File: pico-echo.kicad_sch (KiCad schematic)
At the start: 51 parts, among them J1 USB_C_Receptacle_USB2.0, J2 I2C, J4 Conn_01x16, J5 Conn_01x12, J6 BAT, Q1 BSS83P, SW1 SW_Push, SW2 SW_Push, U1 RP2040, U2 W25Q128JVS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

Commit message: Updated tracks, not finished yet
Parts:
- D2: footprint Capacitor_SMD:C_0603_1608Metric -> LED_SMD:LED_0603_1608Metric
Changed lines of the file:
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@@
 			)
 		)
-		(property "Footprint" "Capacitor_SMD:C_0603_1608Metric"
+		(property "Footprint" "LED_SMD:LED_0603_1608Metric"
 			(at 107.95 39.37 0)
 			(effects

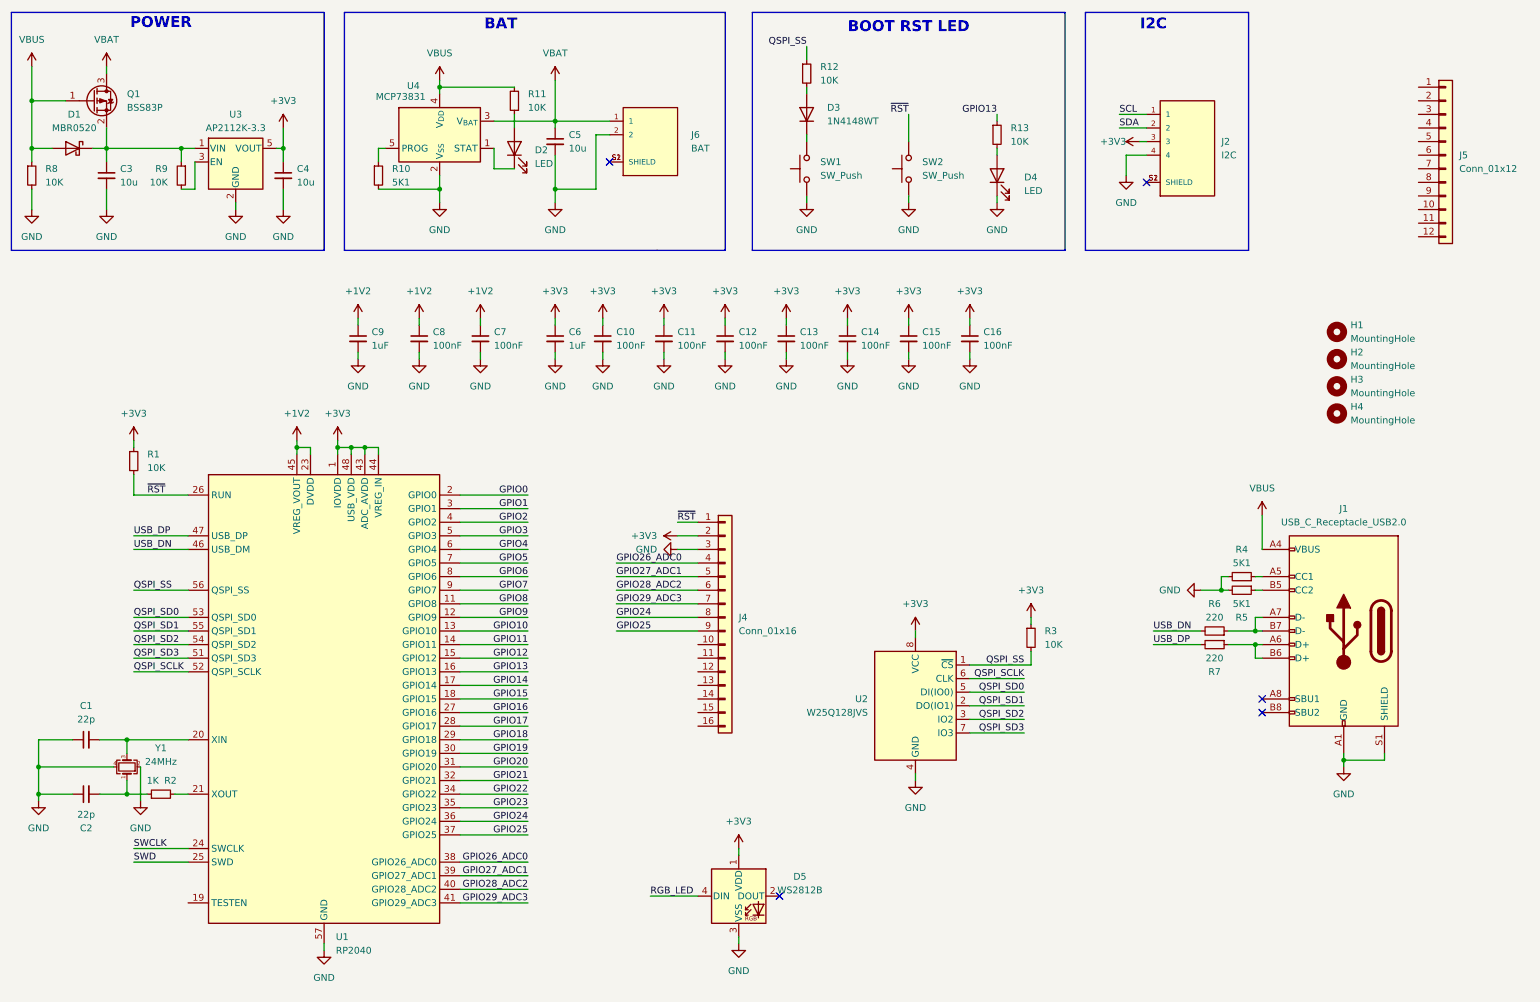
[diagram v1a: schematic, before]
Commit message: Add SWD conn, change Flash to USON, tracks almost finished
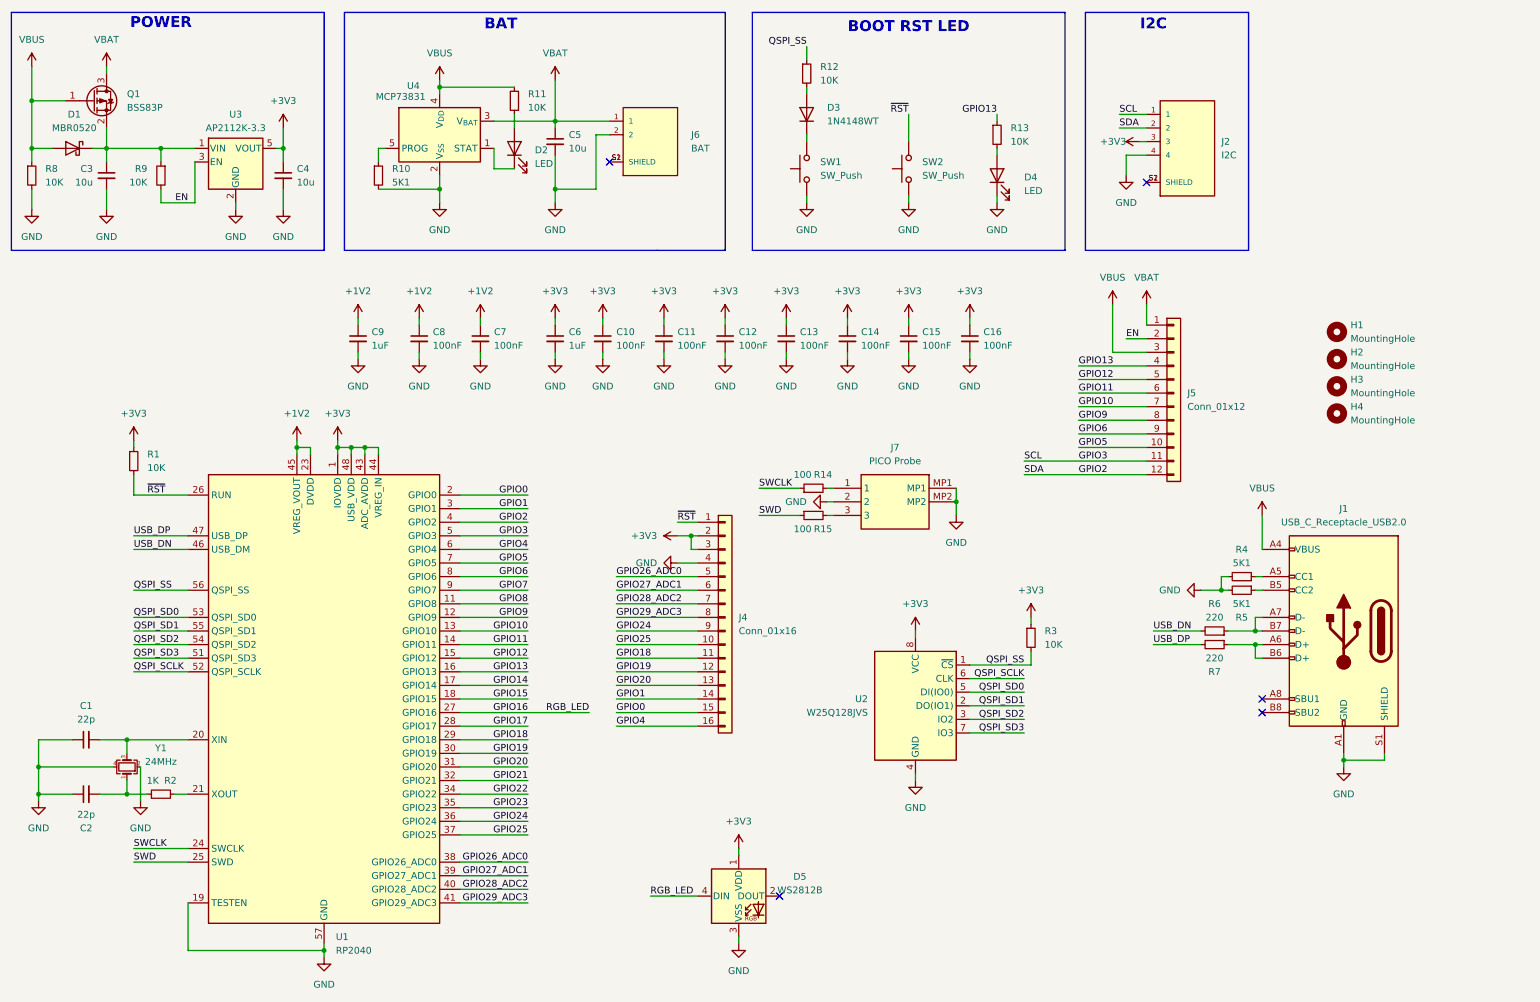
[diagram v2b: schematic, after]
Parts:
- added J7: PICO Probe, BM03B-SRSS-TBT_LF__SN_:BM03BSRSSTBTLFSN, symbol BM03B-SRSS-TBT_LF__SN_:BM03B-SRSS-TBT_LF__SN_
- added R14, R15: 100, Resistor_SMD:R_0402_1005Metric, symbol Device:R_Small
- D5: footprint LED_SMD:LED_WS2812B-2020_PLCC4_2.0x2.0mm -> LED_SMD:LED_SK6805_PLCC4_2.4x2.7mm_P1.3mm
- U2: footprint Package_SO:SOIC-8_5.23x5.23mm_P1.27mm -> SPI-Flash:USON-8-3x4
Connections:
- net RGB_LED is gone; now on net GPIO16: D5.4 (DIN)
- net SCL is gone; now on net GPIO3: J2.1
- net SDA is gone; now on net GPIO2: J2.2
- net +3V3: now also J4.3 (Pin_3)
- net GND: now also J4.4 (Pin_4), U1.19 (TESTEN), J7.2, J7.MP1, J7.MP2; no longer J4.3 (Pin_3)
- net GPIO0: now also J4.15 (Pin_15)
- net GPIO1: now also J4.14 (Pin_14)
- net GPIO10: now also J5.7 (Pin_7)
- net GPIO11: now also J5.6 (Pin_6)
- net GPIO12: now also J5.5 (Pin_5)
- net GPIO13: now also J5.4 (Pin_4)
- net GPIO18: now also J4.11 (Pin_11)
- net GPIO19: now also J4.12 (Pin_12)
- net GPIO2: now also J5.12 (Pin_12)
- net GPIO20: now also J4.13 (Pin_13)
- net GPIO24: now also J4.9 (Pin_9); no longer J4.8 (Pin_8)
- net GPIO25: now also J4.10 (Pin_10); no longer J4.9 (Pin_9)
- net GPIO26_ADC0: now also J4.5 (Pin_5); no longer J4.4 (Pin_4)
- net GPIO27_ADC1: now also J4.6 (Pin_6); no longer J4.5 (Pin_5)
- net GPIO28_ADC2: now also J4.7 (Pin_7); no longer J4.6 (Pin_6)
- net GPIO29_ADC3: now also J4.8 (Pin_8); no longer J4.7 (Pin_7)
- net GPIO3: now also J5.11 (Pin_11)
- net GPIO4: now also J4.16 (Pin_16)
- net GPIO5: now also J5.10 (Pin_10)
- net GPIO6: now also J5.9 (Pin_9)
- net GPIO9: now also J5.8 (Pin_8)
- net SWCLK: now also R14.1
- net SWD: now also R15.1
- net VBAT: now also J5.1 (Pin_1)
- net VBUS: now also J5.3 (Pin_3)
- net EN: now reaches R9.2, U3.3 (EN)
- net EN: now also J5.2 (Pin_2)
- new net: J7.3, R15.2
- new net: J7.1, R14.2
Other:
- moved on the sheet: J5, R9

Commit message: Finished tracks
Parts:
- added C17: 1uF, Capacitor_SMD:C_0603_1608Metric, symbol Device:C_Small
- D1: value MBR0520 -> MBR0540; footprint Diode_SMD:D_SOD-110 -> Diode_SMD:D_SOD-123
- D3: value 1N4148WT -> NSR0320; footprint Diode_SMD:D_SOD-523 -> Diode_SMD:D_SOD-323_HandSoldering
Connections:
- net +3V3: now also C17.1
- net GND: now also C17.2
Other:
- moved on the sheet: C7, C8, C9

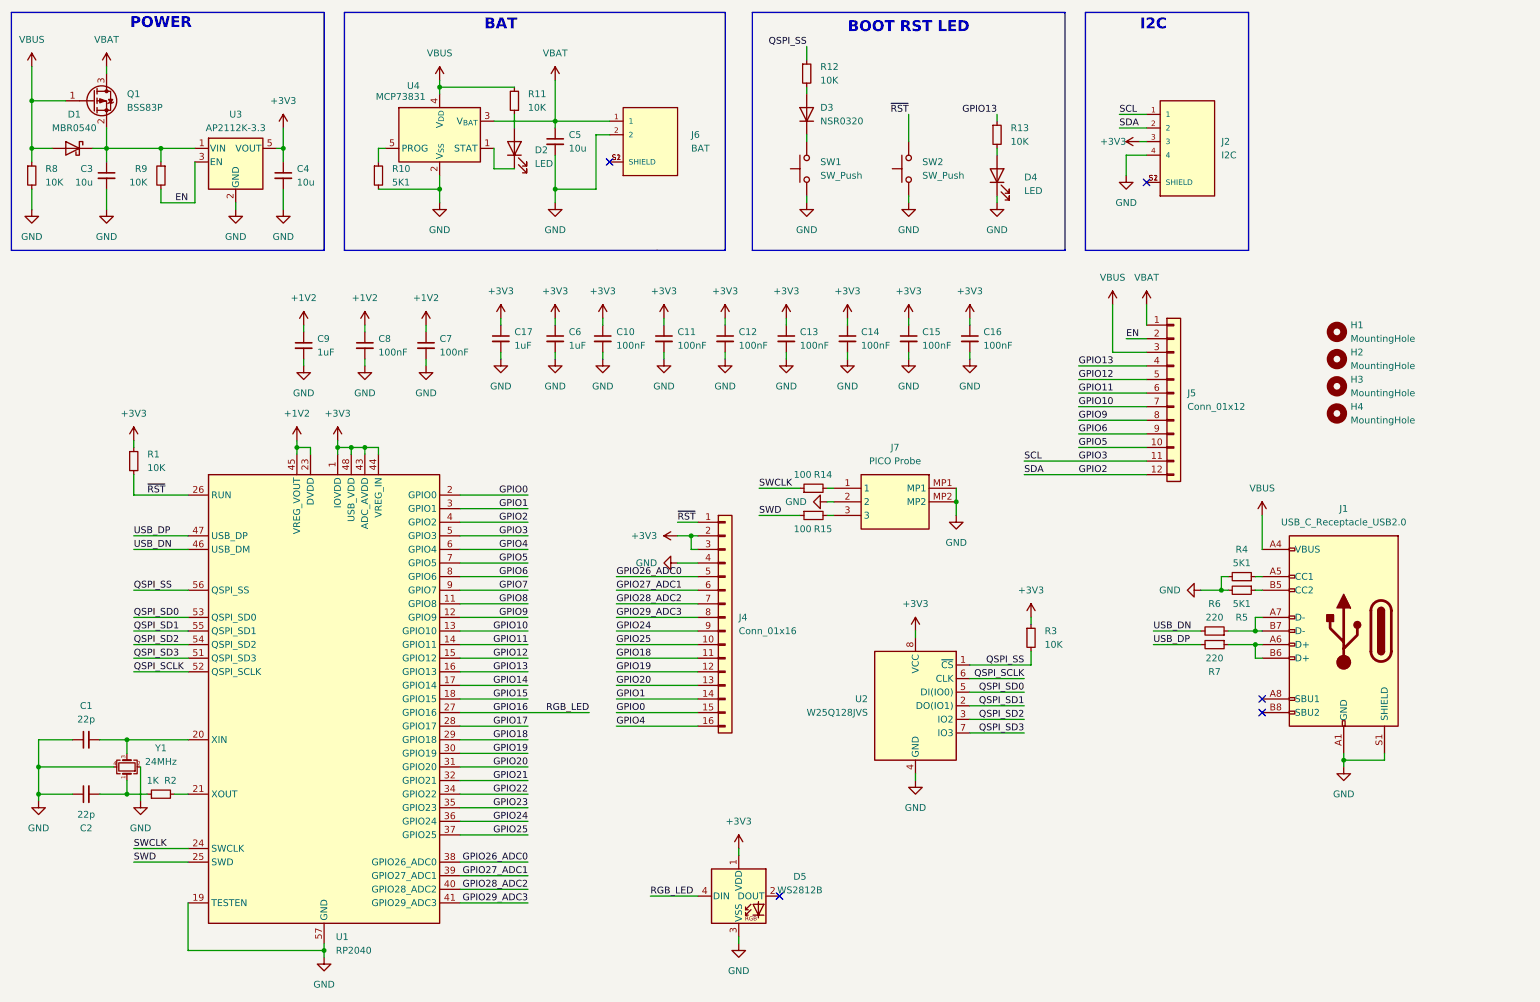
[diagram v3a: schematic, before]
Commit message: Added github repo qrcode logo
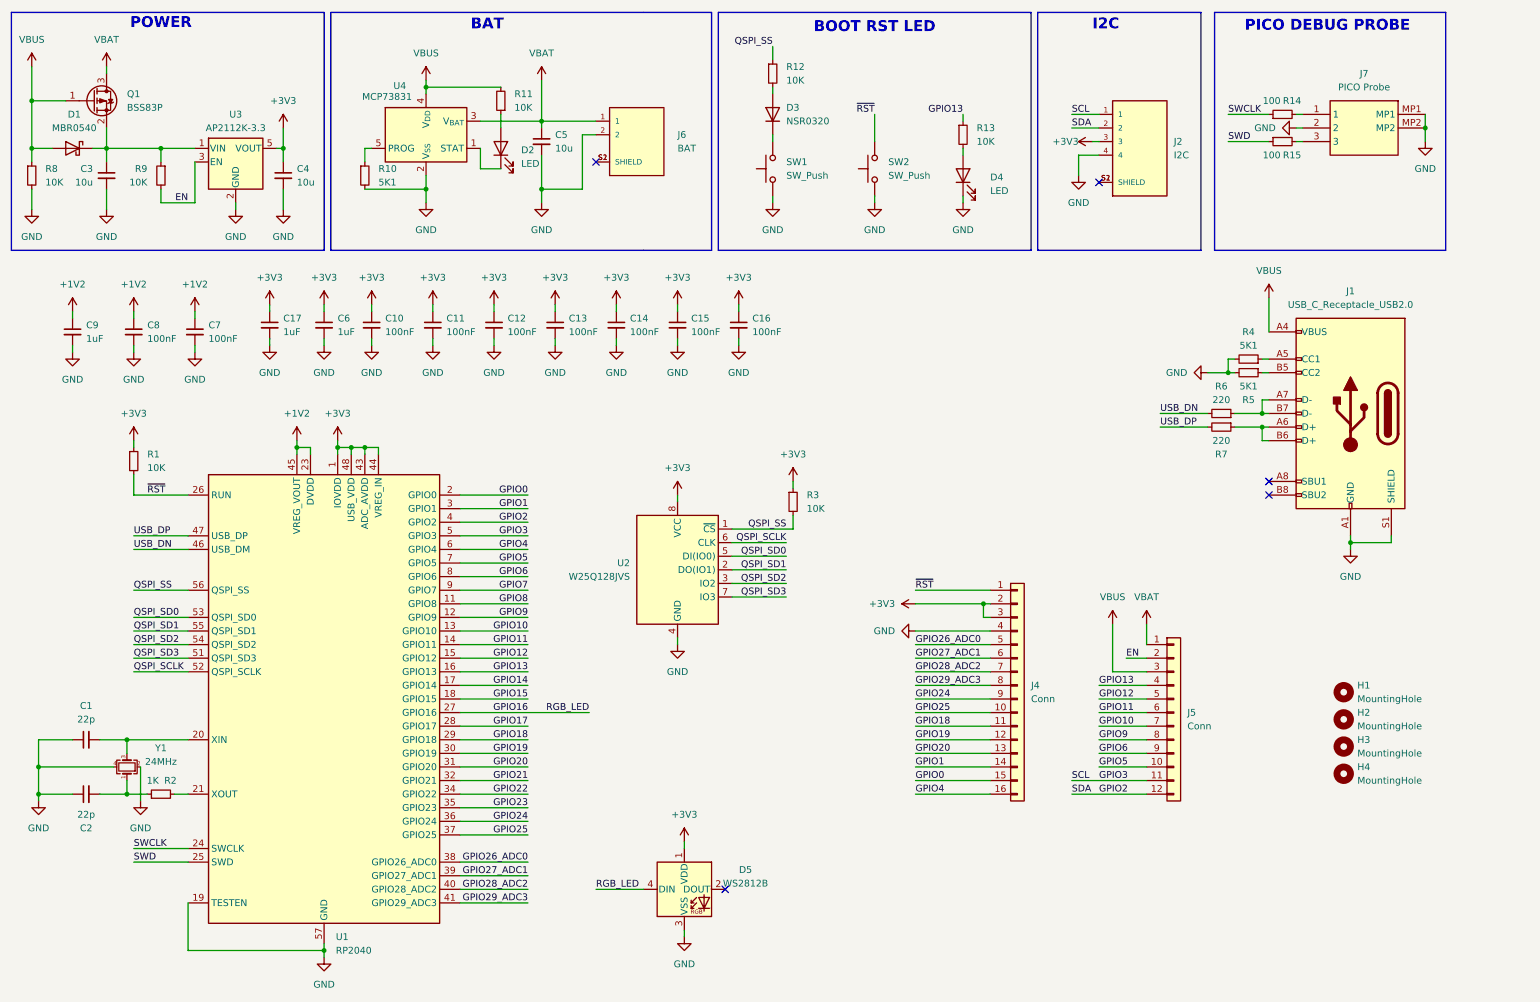
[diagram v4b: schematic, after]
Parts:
- J4: value Conn_01x16 -> Conn
- J5: value Conn_01x12 -> Conn
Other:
- note added: "PICO DEBUG PROBE"
- moved on the sheet: C10, C11, C12, C13, C14, C15, C16, C17, C5, C6, C7, C8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
